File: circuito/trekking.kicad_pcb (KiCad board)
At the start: 2 copper layers, 100 x 100 mm, 4 parts

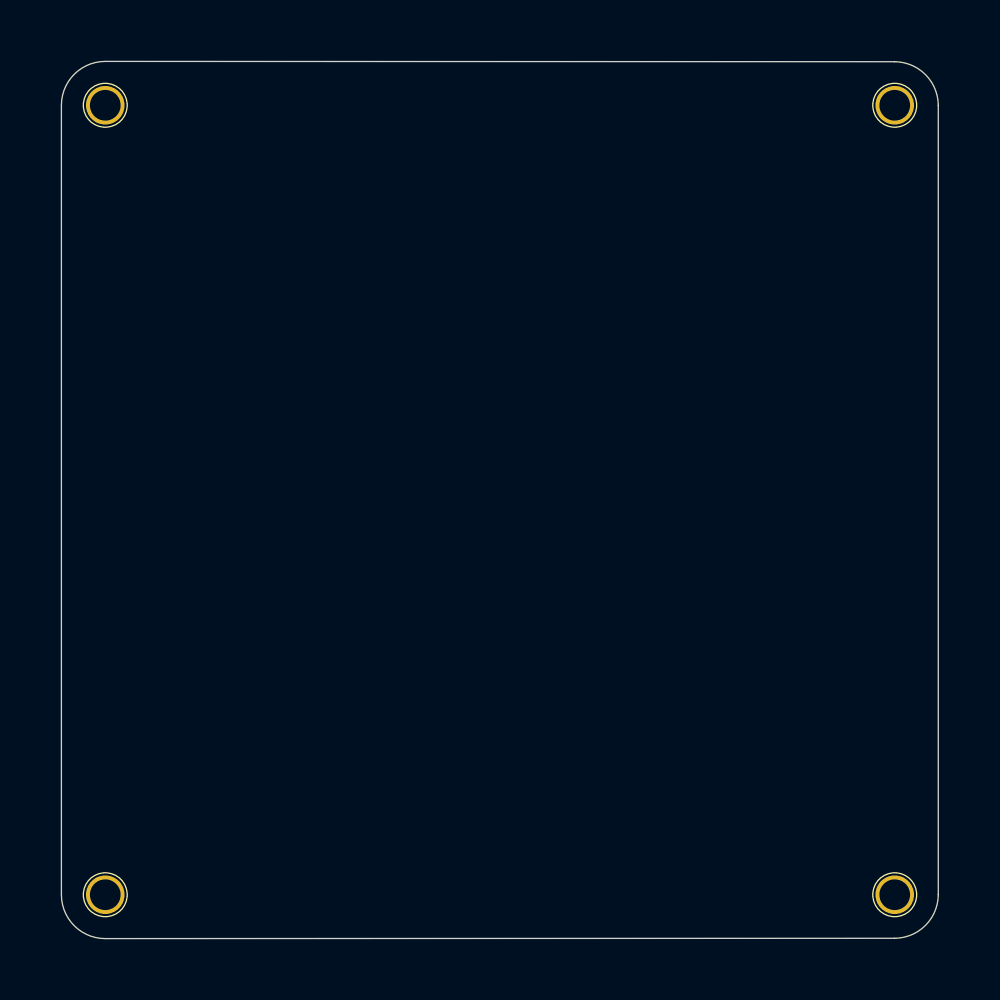
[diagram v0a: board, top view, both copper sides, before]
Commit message: cirando circuito
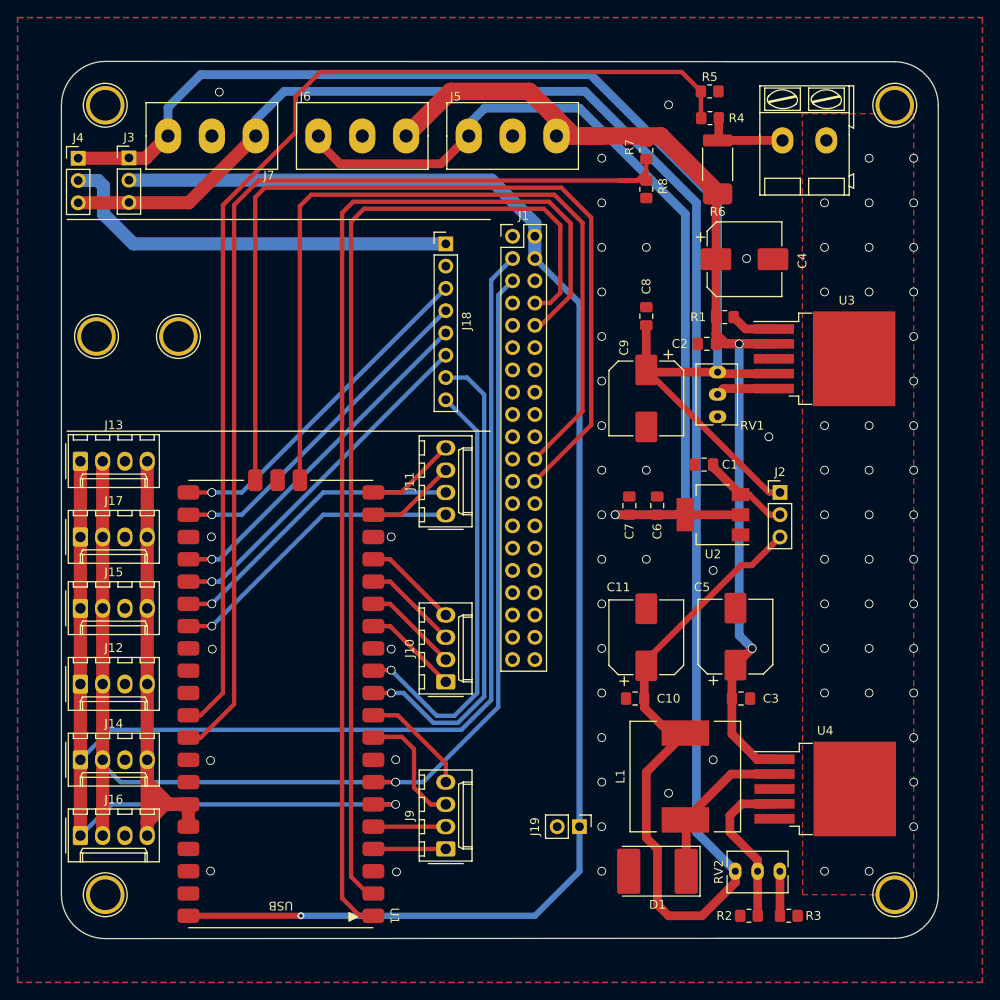
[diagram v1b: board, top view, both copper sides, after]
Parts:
- added C1: 100nF, Capacitor_SMD:C_0805_2012Metric_Pad1.18x1.45mm_HandSolder, F.Cu at (113.3, 101.0)
- added C10: 100nF, Capacitor_SMD:C_0805_2012Metric_Pad1.18x1.45mm_HandSolder, F.Cu at (105.4, 127.6)
- added C11: 220uF35V, Capacitor_SMD:CP_Elec_8x10, F.Cu at (106.7, 120.7)
- added C2: 100nF, Capacitor_SMD:C_0805_2012Metric_Pad1.18x1.45mm_HandSolder, F.Cu at (113.6, 87.2)
- added C3: 100nF, Capacitor_SMD:C_0805_2012Metric_Pad1.18x1.45mm_HandSolder, F.Cu at (117.5, 127.6)
- added C4: 100uF50V, Capacitor_SMD:CP_Elec_8x10, F.Cu at (117.9, 77.5)
- added C5: 100uF50V, Capacitor_SMD:CP_Elec_8x10, F.Cu at (116.8, 120.6)
- added C6: 100nF, Capacitor_SMD:C_0805_2012Metric_Pad1.18x1.45mm_HandSolder, F.Cu at (107.9, 105.6)
- added C7: 10uF6V3, Capacitor_SMD:C_0805_2012Metric_Pad1.18x1.45mm_HandSolder, F.Cu at (104.8, 105.6)
- added C8: 100nF, Capacitor_SMD:C_0805_2012Metric_Pad1.18x1.45mm_HandSolder, F.Cu at (106.7, 84.1)
- added C9: 220uF35V, Capacitor_SMD:CP_Elec_8x10, F.Cu at (106.7, 93.4)
- added D1: 1N5822, Diode_SMD:D_3220_8050Metric_Pad2.65x5.15mm_HandSolder, F.Cu at (108.0, 147.3)
- added J1: Raspberry Pi, Connector_PinHeader_2.54mm:PinHeader_2x20_P2.54mm_Vertical, F.Cu at (91.4, 74.9)
- added J10: P2, Connector_Molex:Molex_KK-254_AE-6410-04A_1x04_P2.54mm_Vertical, F.Cu at (83.8, 125.7)
- added J11: P3, Connector_Molex:Molex_KK-254_AE-6410-04A_1x04_P2.54mm_Vertical, F.Cu at (83.8, 106.7)
- added J12: P3, Connector_Molex:Molex_KK-254_AE-6410-04A_1x04_P2.54mm_Vertical, F.Cu at (42.2, 126.0)
- added J13: P3, Connector_Molex:Molex_KK-254_AE-6410-04A_1x04_P2.54mm_Vertical, F.Cu at (42.2, 100.6)
- added J14: P3, Connector_Molex:Molex_KK-254_AE-6410-04A_1x04_P2.54mm_Vertical, F.Cu at (42.2, 134.6)
- added J15: P3, Connector_Molex:Molex_KK-254_AE-6410-04A_1x04_P2.54mm_Vertical, F.Cu at (42.2, 117.3)
- added J16: P3, Connector_Molex:Molex_KK-254_AE-6410-04A_1x04_P2.54mm_Vertical, F.Cu at (42.2, 143.3)
- added J17: P3, Connector_Molex:Molex_KK-254_AE-6410-04A_1x04_P2.54mm_Vertical, F.Cu at (42.2, 109.2)
- added J18: Module, Connector_PinHeader_2.54mm:PinHeader_1x08_P2.54mm_Vertical, F.Cu at (83.8, 75.8)
- added J19: FAM, Connector_PinHeader_2.54mm:PinHeader_1x02_P2.54mm_Vertical, F.Cu at (99.1, 142.2)
- added J2: V1-X-V2, Connector_PinHeader_2.54mm:PinHeader_1x03_P2.54mm_Vertical, F.Cu at (121.9, 104.1)
- added J3: RAP-SELECT, Connector_PinHeader_2.54mm:PinHeader_1x03_P2.54mm_Vertical, F.Cu at (47.7, 66.0)
- added J4: MOD-SELECT, Connector_PinHeader_2.54mm:PinHeader_1x03_P2.54mm_Vertical, F.Cu at (41.9, 66.0)
- added J5: VOUT-M, MyFootprint:CONN5mm-3, F.Cu at (86.4, 63.5)
- added J6: VOUT-M, MyFootprint:CONN5mm-3, F.Cu at (69.3, 63.5)
- added J7: VOUT-C, MyFootprint:CONN5mm-3, F.Cu at (62.1, 63.5)
- added J8: VIN, MyFootprint:AK300-2, F.Cu at (122.2, 64.0)
- added J9: P1, Connector_Molex:Molex_KK-254_AE-6410-04A_1x04_P2.54mm_Vertical, F.Cu at (83.8, 144.8)
- added L1: 33uH, Inductor_SMD:L_12x12mm_H8mm, F.Cu at (111.1, 136.5)
- added R1: 51k, Resistor_SMD:R_0805_2012Metric_Pad1.20x1.40mm_HandSolder, F.Cu at (115.6, 84.2)
- added R2: 5K, Resistor_SMD:R_0805_2012Metric_Pad1.20x1.40mm_HandSolder, F.Cu at (118.4, 152.4)
- added R3: 0R, Resistor_SMD:R_0805_2012Metric_Pad1.20x1.40mm_HandSolder, F.Cu at (122.9, 152.4)
- added R4: 10k, Resistor_SMD:R_0805_2012Metric_Pad1.20x1.40mm_HandSolder, F.Cu at (113.9, 61.5)
- added R5: 1k, Resistor_SMD:R_0805_2012Metric_Pad1.20x1.40mm_HandSolder, F.Cu at (113.9, 58.4)
- added R6: 0.15R, MyFootprint:R_2512_6332Metric_Pad1.40x3.35mm_HandSolder, F.Cu at (114.8, 67.1)
- added R7: 10k, Resistor_SMD:R_0805_2012Metric_Pad1.20x1.40mm_HandSolder, F.Cu at (106.7, 65.1)
- added R8: 10k, Resistor_SMD:R_0805_2012Metric_Pad1.20x1.40mm_HandSolder, F.Cu at (106.7, 69.6)
- added REF**: Pin_D1.0mm_L10.0mm, MyFootprint:Pin_D3.5mm_L4.4mm, F.Cu at (53.3, 86.4)
- added REF**: Pin_D1.0mm_L10.0mm, MyFootprint:Pin_D3.5mm_L4.4mm, F.Cu at (44.0, 86.4)
- added RV1: 10k, Potentiometer_THT:Potentiometer_Bourns_3266Y_Vertical, F.Cu at (114.8, 95.5)
- added RV2: 10k, Potentiometer_THT:Potentiometer_Bourns_3266Y_Vertical, F.Cu at (121.9, 147.3)
- added U1: RPI-PICO, MyFootprint:RPI-PICO-SMD, F.Cu at (75.5, 102.8)
- added U2: AMS1117-3.3, Package_TO_SOT_SMD:SOT-223-3_TabPin2, F.Cu at (114.3, 106.7)
- added U3: MIC29302WU, Package_TO_SOT_SMD:TO-263-5_TabPin3, F.Cu at (127.0, 88.9)
- added U4: LM2596S-ADJ, Package_TO_SOT_SMD:TO-263-5_TabPin3, F.Cu at (127.1, 137.9)
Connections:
- REF** pad 1: (no net) -> Earth (x4)
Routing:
- net /V1: track 0.00 -> 226.1 mm
- net /SDA0: track 0.00 -> 183.6 mm, vias 0 -> 1
- net +5V: track 0.00 -> 171.3 mm, vias 0 -> 1
- net /SCL0: track 0.00 -> 144.5 mm, vias 0 -> 1
- net /V2: track 0.00 -> 144.4 mm
- net VCC: track 0.00 -> 134.2 mm, vias 0 -> 2
- net /ADC0: track 0.00 -> 127.7 mm
- net /TXD0: track 0.00 -> 123.8 mm
- net /ADC1: track 0.00 -> 117.8 mm
- net /RXD0: track 0.00 -> 114.3 mm
- net /V3: track 0.00 -> 108.1 mm, vias 0 -> 1
- net /SWDIO: track 0.00 -> 105.1 mm
- net /SWCLK: track 0.00 -> 94.5 mm
- net +3V3: track 0.00 -> 63.8 mm
- net /TXD1: track 0.00 -> 54.9 mm, vias 0 -> 1
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- added copper zone on B.Cu, net Earth
- added copper zone on F.Cu, net Earth

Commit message: circuiro rev 1.0
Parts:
- added G***: LOGO, MyFootprint:LOGO3, F.Cu at (133.1, 100.7)
- added REF**: ESD-Logo_6.6x6mm_SilkScreen, Symbol:ESD-Logo_6.6x6mm_SilkScreen, F.Cu at (133.6, 122.0)
- added REF**: WEEE-Logo_5.6x8mm_SilkScreen, Symbol:WEEE-Logo_5.6x8mm_SilkScreen, F.Cu at (97.0, 150.5)
- added REF**: OSHW-Logo2_7.3x6mm_SilkScreen, Symbol:OSHW-Logo2_7.3x6mm_SilkScreen, F.Cu at (88.4, 151.5)
- J12, J13, J14, J15, J16, J17: value P3 -> I2C0
- moved REF** 8.94 mm to (45.7, 91.0)
- moved REF** 8.20 mm to (45.7, 78.3)
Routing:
- net Earth: vias 74 -> 98
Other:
- board text added: "3V3"
- board text added: "5V"
- board text added: "G10"
- board text added: "G11"
- board text added: "G12"
- board text added: "G13"
- board text added: "G14"
- board text added: "G15"
- board text added: "G16"
- board text added: "G17"
- board text added: "G18"
- board text added: "G19"
- board text added: "G2"
- board text added: "G20"
- board text added: "G21"
- board text added: "G3"
- board text added: "G6"
- board text added: "G7"
- board text added: "G8"
- board text added: "G9"
- board text added: "GND"
- board text added: "MOD"
- board text added: "RPI"
- board text added: "RPI DEVE SER 5V"
- board text added: "RXD0"
- board text added: "RXD1"
- board text added: "S0RX"
- board text added: "S0SC"
- board text added: "S0SCK"
- board text added: "S0TX"
- board text added: "SCL0"
- board text added: "SDA0"
- board text added: "SWCLK"
- board text added: "SWDIO"
- board text added: "TREKKING 2022 REV 1.0 By @pedro_ibs"
- board text added: "TXD0"
- board text added: "TXD1"
- board text added: "V1"
- board text added: "V1 AJUSTÁVEL V2 AJUSTÁVEL V3 3V3"
- board text added: "V2"
- board text added: "V3"
- board text added: "V3-IN"
- board text added: "VCC"
- board text added: "VIN"
- board text added: "Vmod"

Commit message: circuiro rev 1.0 correção
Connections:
- J1 pad 18: unconnected-(J1-Pad18) -> /SWDIO
- J1 pad 24: /SWDIO -> unconnected-(J1-Pad24)
- J1 pad 7: /CTRL_RUN -> unconnected-(J1-Pad7)
- U1 pad 30: /RUN -> unconnected-(U1-Pad30)
- U1 pad 34: /ADC2 -> unconnected-(U1-Pad34)
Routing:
- net /SWDIO: track 105.1 -> 110.7 mm, vias 0 -> 1
- net /V2: track 144.4 -> 142.7 mm
- net /SWCLK: track 94.5 -> 96.0 mm
- net Earth: vias 98 -> 101

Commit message: ATT placa fontes e pinos de contole
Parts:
- removed J3: RAP-SELECT, Connector_PinHeader_2.54mm:PinHeader_1x03_P2.54mm_Vertical
- removed RV2: 10k, Potentiometer_THT:Potentiometer_Bourns_3266Y_Vertical
- added ?: , , F.Cu at (47.2, 71.1)
- added J**: HOLE, MyFootprint:HOLE, F.Cu at (47.2, 66.0)
- R2: value 5K -> 10k
- R3: value 0R -> 1k
- moved R3 72.9 mm to (50.1, 150.0)
- moved R2 68.3 mm to (50.1, 152.5)
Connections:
- C10 pad 1: /V1 -> +5V
- C11 pad 1: /V1 -> +5V
- J1 pad 29: unconnected-(J1-Pad29) -> /G22
- J1 pad 31: unconnected-(J1-Pad31) -> /RUN
- J2 pad 3: /V1 -> +5V
- J4 pad 3: /V1 -> +5V
- J7 pad 1: /V1 -> +5V
- L1 pad 2: /V1 -> +5V
- R2 pad 1: Net-(R2-Pad1) -> +5V
- R2 pad 2: Earth -> /ADC2
- R3 pad 1: Net-(R3-Pad1) -> /ADC2
- U1 pad 29: unconnected-(U1-Pad29) -> /G22
- U1 pad 30: unconnected-(U1-Pad30) -> /RUN
- U1 pad 34: unconnected-(U1-Pad34) -> /ADC2
- U4 pad 4: Net-(R2-Pad1) -> +5V
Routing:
- net +5V: track 171.3 -> 400.0 mm, vias 1 -> 2
- net /V1: track 226.1 -> 0.00 mm
- net /RUN: track 0.00 -> 43.6 mm, vias 0 -> 2
- net /G22: track 0.00 -> 42.7 mm, vias 0 -> 2
- net /ADC2: track 0.00 -> 24.1 mm, vias 0 -> 2
- net Net-(R2-Pad1): track 18.4 -> 0.00 mm
- net Net-(R3-Pad1): track 5.09 -> 0.00 mm
- net Vmod: track 46.8 -> 44.9 mm
- net /ADC1: track 117.8 -> 119.3 mm
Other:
- board text added: "G22-G5"
- board text added: "RUN-G6"
- board text added: "V1 5V"
- board text added: "V1 5V V2 AJUSTÁVEL V3 3V3"
- board text added: "V3 3V3"
- board text removed: "RPI"
- board text removed: "RPI DEVE SER 5V"
- board text removed: "V1 AJUSTÁVEL V2 AJUSTÁVEL V3 3V3"
- board text removed: "V3"
